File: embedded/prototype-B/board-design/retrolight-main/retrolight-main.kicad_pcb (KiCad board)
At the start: 2 copper layers, 75 x 25 mm, 43 parts, among them J1 Conn_02x03_Odd_Even, U1 TLC59108xPW, U2 TLC59108xPW

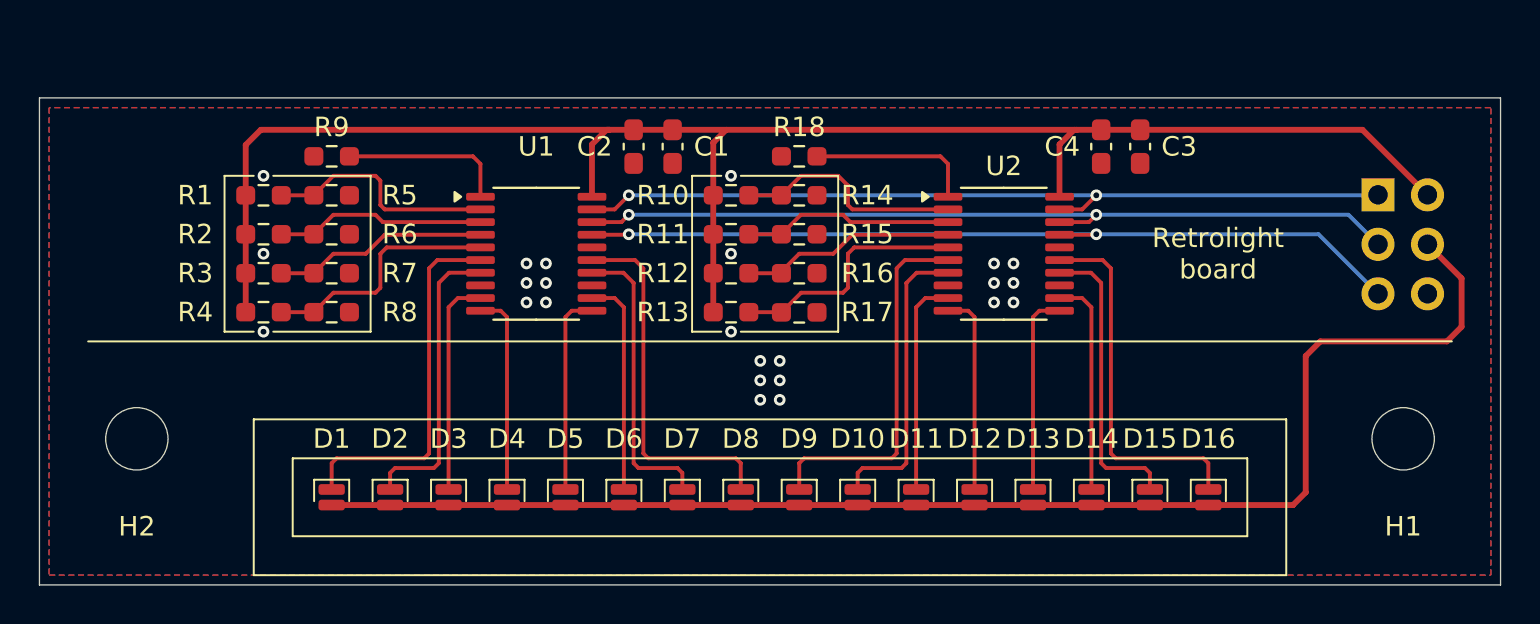
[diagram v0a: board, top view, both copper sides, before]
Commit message: [Refactored PCB design]
Renewed PCB design for the retrolight app.

Signed-off-by: Nicolae-Andrei Vasile <vasilenicolaeandrei@gmail.com>
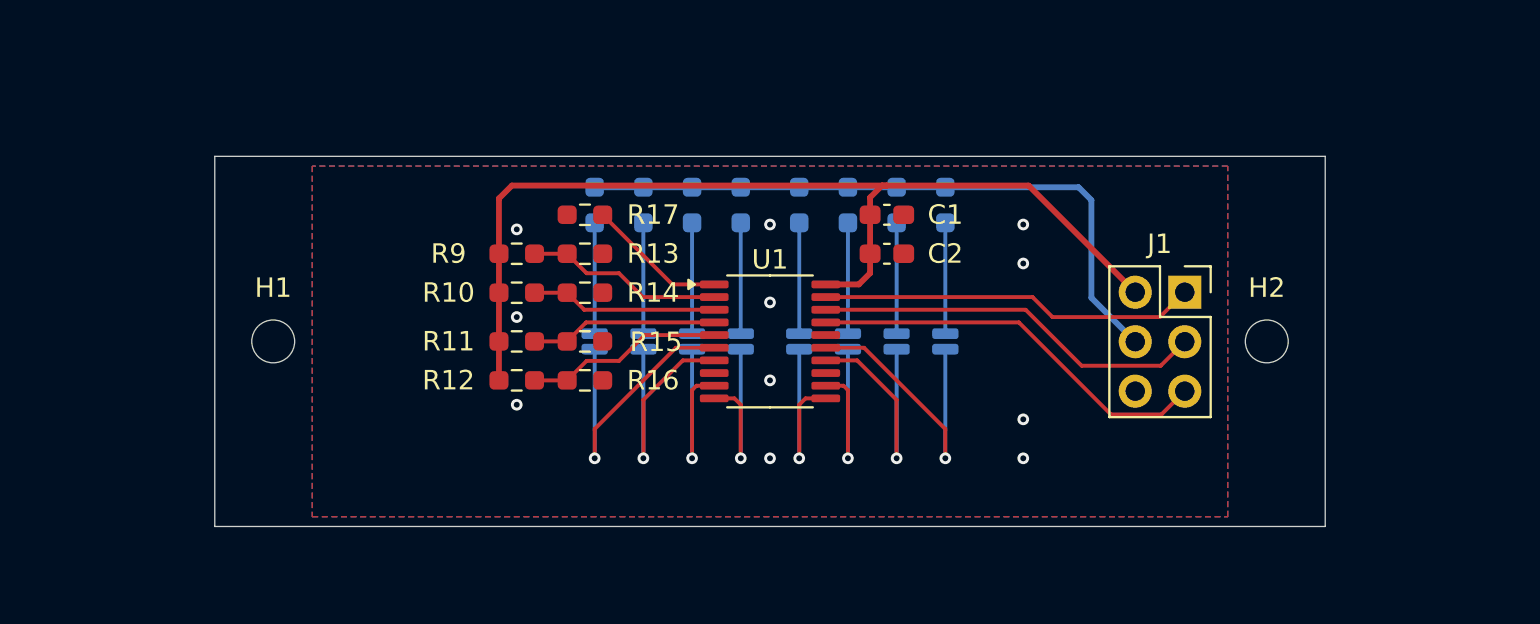
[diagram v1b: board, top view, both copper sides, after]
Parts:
- removed C3: 10uF/6.3V/20%/C0603, Capacitor_SMD:C_0603_1608Metric_Pad1.08x0.95mm_HandSolder
- removed C4: 100nF/6.3V/20%/C0603, Capacitor_SMD:C_0603_1608Metric_Pad1.08x0.95mm_HandSolder
- removed D10, D11, D12, D13, D14, D15, D16, D9: LED, LED:LED_0505_1313Metric
- removed R18: 375R/R0603, Resistor_SMD:R_0603_1608Metric_Pad0.98x0.95mm_HandSolder
- removed U2: TLC59108xPW, Package_SO:TSSOP-20_4.4x6.5mm_P0.65mm
- D1, D2, D3, D4, D5, D6, D7, D8, R5, R6, R7, R8: moved to B.Cu
- H1, H2: footprint MountingHole:MountingHole_3.2mm_M3 -> MountingHole:MountingHole_2.2mm_M2_ISO7380
- J1: moved to F.Cu
- R1, R2, R3, R4: value 10K/R0603(NC) -> 0R/R0603; moved to B.Cu
- R13: value 10K/R0603(NC) -> 0R/R0603
- R17: value 0R/R0603 -> 375R/R0603
- R9: value 375R/R0603 -> 10K/R0603(NC)
- moved H1 58.2 mm to (124.5, 100.0)
- moved H2 58.2 mm to (175.5, 100.0)
- moved R8 32.0 mm to (159.0, 93.0), turned to 90 degrees
- moved R7 29.2 mm to (156.5, 93.0), turned to 90 degrees
- moved R6 26.5 mm to (154.0, 93.0), turned to 90 degrees
- moved R4 25.1 mm to (148.5, 93.0), turned to 90 degrees
- moved R5 24.0 mm to (151.5, 93.0), turned to 90 degrees
- moved R3 22.3 mm to (146.0, 93.0), turned to 90 degrees
- moved R2 19.6 mm to (143.5, 93.0), turned to 90 degrees
- moved R1 17.0 mm to (141.0, 93.0), turned to 90 degrees
- moved D1 15.7 mm to (141.0, 100.0), turned to 90 degrees
- moved D2 15.3 mm to (143.5, 100.0), turned to 90 degrees
- moved D3 14.8 mm to (146.0, 100.0), turned to 90 degrees
- moved D4 14.4 mm to (148.5, 100.0), turned to 90 degrees
- moved D5 14.4 mm to (151.5, 100.0), turned to 90 degrees
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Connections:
- D1 pad 2: VLED -> Net-(D1-A)
- D2 pad 2: VLED -> Net-(D2-A)
- D3 pad 2: VLED -> Net-(D3-A)
- D4 pad 2: VLED -> Net-(D4-A)
- D5 pad 2: VLED -> Net-(D5-A)
- D6 pad 2: VLED -> Net-(D6-A)
- D7 pad 2: VLED -> Net-(D7-A)
- D8 pad 2: VLED -> Net-(D8-A)
- R1 pad 1: Net-(U1-A0) -> Net-(D1-A)
- R1 pad 2: VCC -> VLED
- R10 pad 1: Net-(U2-A0) -> Net-(U1-A1)
- R11 pad 1: Net-(U2-A1) -> Net-(U1-A2)
- R12 pad 1: Net-(U2-A2) -> Net-(U1-A3)
- R13 pad 1: Net-(U2-A3) -> Net-(U1-A0)
- R13 pad 2: VCC -> GND
- R14 pad 1: Net-(U2-A0) -> Net-(U1-A1)
- R15 pad 1: Net-(U2-A1) -> Net-(U1-A2)
- R16 pad 1: Net-(U2-A2) -> Net-(U1-A3)
- R17 pad 1: Net-(U2-A3) -> Net-(U1-REXT)
- R2 pad 1: Net-(U1-A1) -> Net-(D2-A)
- R2 pad 2: VCC -> VLED
- R3 pad 1: Net-(U1-A2) -> Net-(D3-A)
- R3 pad 2: VCC -> VLED
- R4 pad 1: Net-(U1-A3) -> Net-(D4-A)
- R4 pad 2: VCC -> VLED
- R5 pad 1: Net-(U1-A0) -> Net-(D5-A)
- R5 pad 2: GND -> VLED
- R6 pad 1: Net-(U1-A1) -> Net-(D6-A)
- R6 pad 2: GND -> VLED
- R7 pad 1: Net-(U1-A2) -> Net-(D7-A)
- R7 pad 2: GND -> VLED
- R8 pad 1: Net-(U1-A3) -> Net-(D8-A)
- R8 pad 2: GND -> VLED
- R9 pad 1: Net-(U1-REXT) -> Net-(U1-A0)
- R9 pad 2: GND -> VCC
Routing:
- net VLED: track 70.9 -> 34.0 mm
- net VCC: track 88.2 -> 52.1 mm
- net /SDA: track 42.8 -> 19.4 mm, vias 2 -> 0
- net /SCL: track 43.2 -> 20.1 mm, vias 2 -> 0
- net /~{RESET}: track 43.5 -> 20.9 mm, vias 2 -> 0
- net Net-(D16-K): track 18.9 -> 0.00 mm
- net Net-(D9-K): track 18.9 -> 0.00 mm
- net Net-(D15-K): track 15.2 -> 0.00 mm
- net Net-(D10-K): track 15.2 -> 0.00 mm
- net Net-(U2-A3): track 12.6 -> 0.00 mm
- net Net-(U2-A0): track 11.9 -> 0.00 mm
- net Net-(D14-K): track 11.2 -> 0.00 mm
- net Net-(D11-K): track 11.2 -> 0.00 mm
- net Net-(U2-A2): track 11.1 -> 0.00 mm
- net Net-(U2-A1): track 10.8 -> 0.00 mm
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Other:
- board size 75 x 25 mm -> 57 x 19 mm
- board text removed: "Retrolight board"

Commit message: [Light] Rework
Refactored light module design to match the newest changes for the
central unit.

Signed-off-by: Nicolae-Andrei Prodan <vasilenicolaeandrei@gmail.com>
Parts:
- added D9: MBRS130LT3G, Diode_SMD:D_SMB, F.Cu at (156.0, 91.0)
- H1, H2: value MountingHole -> MountingHole_Pad; footprint MountingHole:MountingHole_2.2mm_M2_ISO7380 -> MountingHole:MountingHole_4.3mm_M4_ISO7380_Pad
- J1: value Conn_02x03_Odd_Even -> Conn_02x05_Odd_Even; footprint Connector_PinSocket_2.54mm:PinSocket_2x03_P2.54mm_Vertical -> Connector_IDC:IDC-Header_2x05_P2.54mm_Vertical
- R1, R3, R5, R7: value 0R/R0603 -> 10K/R0603(NC); moved to F.Cu
- R10, R11, R12: value 10K/R0603(NC) -> 0R/R0603; moved to B.Cu
- R13, R14, R15, R16: moved to B.Cu
- R17: value 375R/R0603 -> 0R/R0603; moved to B.Cu
- R2, R4, R6, R8: moved to F.Cu
- R9: value 10K/R0603(NC) -> 375R/R0603
- moved R7 27.0 mm to (129.5, 92.5), turned to 180 degrees
- moved R8 25.5 mm to (133.5, 92.5), turned to 0 degrees
- moved J1 23.7 mm to (147.6, 98.5), turned to -90 degrees
- moved R5 22.1 mm to (129.5, 90.5), turned to 180 degrees
- moved R6 20.7 mm to (133.5, 90.5), turned to 0 degrees
- moved R3 17.2 mm to (129.5, 88.0), turned to 180 degrees
- moved R4 15.8 mm to (133.5, 88.0), turned to 0 degrees
- moved H2 15.5 mm to (160.0, 100.0)
- moved R16 14.7 mm to (149.0, 90.0), turned to 90 degrees
- moved R1 13.5 mm to (129.5, 86.0), turned to 180 degrees
- moved R2 12.2 mm to (133.5, 86.0), turned to 0 degrees
- moved U1 12.1 mm to (142.5, 90.5)
- moved R12 12.1 mm to (138.5, 90.0), turned to 90 degrees
- moved R15 11.7 mm to (146.5, 90.0), turned to 90 degrees
- moved R17 11.5 mm to (151.5, 90.0), turned to 90 degrees
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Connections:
- J1 pad 1: /SDA -> Net-(D9-A)
- J1 pad 2: VCC -> unconnected-(J1-Pin_2-Pad2)
- J1 pad 3: /SCL -> /SDA
- J1 pad 4: VLED -> unconnected-(J1-Pin_4-Pad4)
- J1 pad 5: /~{RESET} -> /SCL
- J1 pad 6: GND -> unconnected-(J1-Pin_6-Pad6)
- R1 pad 1: Net-(D1-A) -> Net-(U1-A0)
- R1 pad 2: VLED -> VCC
- R10 pad 1: Net-(U1-A1) -> Net-(D1-A)
- R11 pad 1: Net-(U1-A2) -> Net-(D2-A)
- R12 pad 1: Net-(U1-A3) -> Net-(D3-A)
- R13 pad 1: Net-(U1-A0) -> Net-(D4-A)
- R13 pad 2: GND -> VCC
- R14 pad 1: Net-(U1-A1) -> Net-(D5-A)
- R14 pad 2: GND -> VCC
- R15 pad 1: Net-(U1-A2) -> Net-(D6-A)
- R15 pad 2: GND -> VCC
- R16 pad 1: Net-(U1-A3) -> Net-(D7-A)
- R16 pad 2: GND -> VCC
- R17 pad 1: Net-(U1-REXT) -> Net-(D8-A)
- R17 pad 2: GND -> VCC
- R2 pad 1: Net-(D2-A) -> Net-(U1-A0)
- R2 pad 2: VLED -> GND
- R3 pad 1: Net-(D3-A) -> Net-(U1-A1)
- R3 pad 2: VLED -> VCC
- R4 pad 1: Net-(D4-A) -> Net-(U1-A1)
- R4 pad 2: VLED -> GND
- R5 pad 1: Net-(D5-A) -> Net-(U1-A2)
- R5 pad 2: VLED -> VCC
- R6 pad 1: Net-(D6-A) -> Net-(U1-A2)
- R6 pad 2: VLED -> GND
- R7 pad 1: Net-(D7-A) -> Net-(U1-A3)
- R7 pad 2: VLED -> VCC
- R8 pad 1: Net-(D8-A) -> Net-(U1-A3)
- R8 pad 2: VLED -> GND
- R9 pad 1: Net-(U1-A0) -> Net-(U1-REXT)
- R9 pad 2: VCC -> GND
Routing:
- net VLED: track 34.0 -> 0.00 mm
- net Net-(D9-A): track 0.00 -> 13.2 mm
- net VCC: track 52.1 -> 44.5 mm, vias 0 -> 2
- net Net-(D5-K): track 9.85 -> 3.59 mm
- net Net-(D4-K): track 9.85 -> 3.59 mm
- net Net-(D6-K): track 10.3 -> 4.39 mm
- net Net-(D3-K): track 10.3 -> 4.39 mm
- net Net-(D7-K): track 13.1 -> 7.16 mm
- net Net-(D2-K): track 13.1 -> 7.16 mm
- net Net-(D8-K): track 15.0 -> 9.64 mm
- net Net-(D1-K): track 15.0 -> 9.64 mm
- net Net-(U1-REXT): track 7.21 -> 1.90 mm
- net Net-(D8-A): track 5.69 -> 1.69 mm
- net Net-(D7-A): track 5.69 -> 1.69 mm
- net Net-(D6-A): track 5.69 -> 1.69 mm
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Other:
- board size 57 x 19 mm -> 45 x 20.5 mm
